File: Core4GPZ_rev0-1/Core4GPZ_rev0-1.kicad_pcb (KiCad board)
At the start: 2 copper layers, 78.7 x 105.2 mm, 50 parts, among them IC1 MAX9926UAEE_V+, M3 MountingHole_3.2mm_M3_DIN965_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, Q1 FGD3440G2-F085, Q2 FGD3440G2-F085, U2 core4, U3 MPXHZ6250AC6T1, U4 LMV321

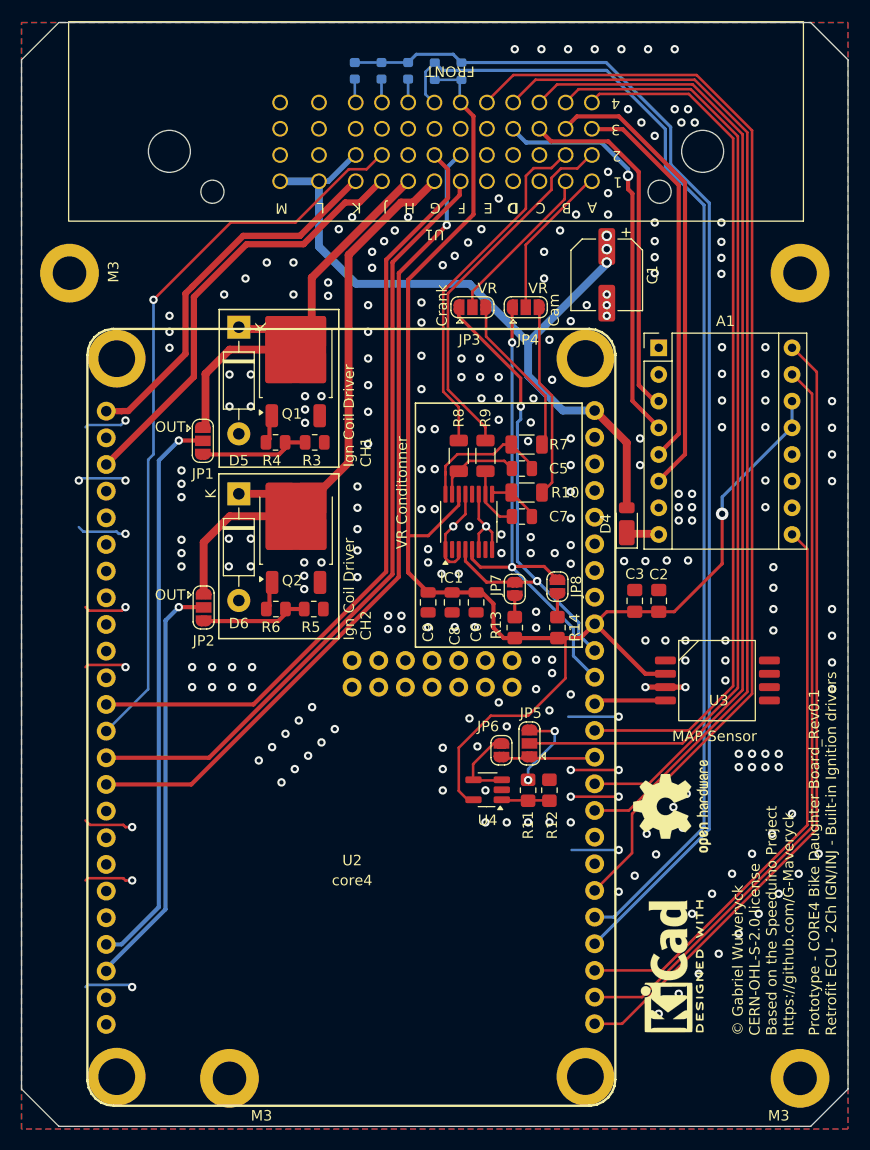
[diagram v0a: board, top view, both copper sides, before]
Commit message: Updated CAD Enclosure STL and STEP export
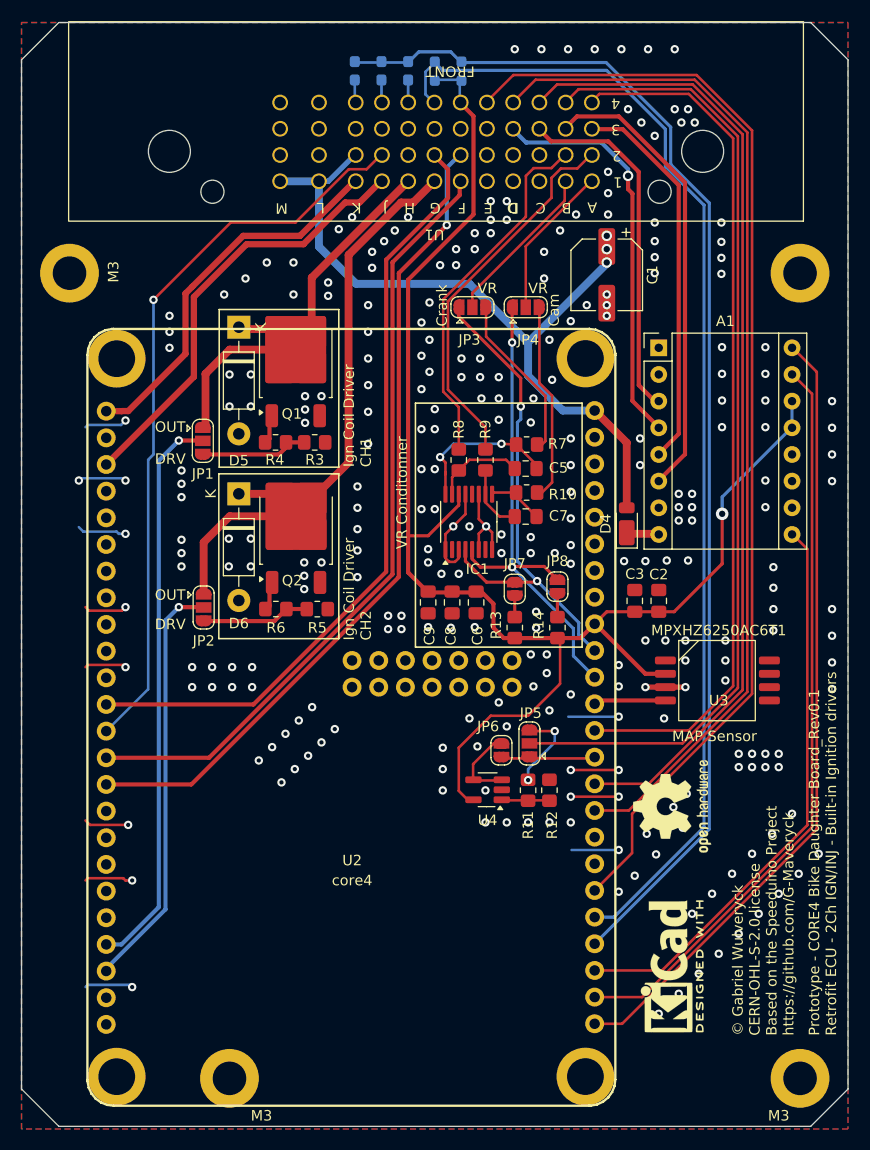
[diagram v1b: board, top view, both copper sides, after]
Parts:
- C5, C6, C7, C8, C9: footprint Capacitor_SMD:C_0805_2012Metric -> Capacitor_SMD:C_0805_2012Metric_Pad1.18x1.45mm_HandSolder
- D1, D2, D3: footprint Diode_SMD:D_0603_1608Metric -> Diode_SMD:D_0603_1608Metric_Pad1.05x0.95mm_HandSolder
- R1, R2: footprint Resistor_SMD:R_0603_1608Metric -> Resistor_SMD:R_0603_1608Metric_Pad0.98x0.95mm_HandSolder
- R10, R7, R8, R9: footprint Resistor_SMD:R_1206_3216Metric -> Resistor_SMD:R_0805_2012Metric_Pad1.20x1.40mm_HandSolder
- R3, R4, R5, R6: footprint Resistor_SMD:R_0805_2012Metric -> Resistor_SMD:R_0805_2012Metric_Pad1.20x1.40mm_HandSolder
- moved R8 0.39 mm to (119.1, 80.4)
- moved R9 0.39 mm to (121.7, 80.4)
- moved C5 0.36 mm to (125.5, 81.2)
- moved C7 0.36 mm to (125.5, 85.8)
- moved R5 0.33 mm to (105.7, 94.6)
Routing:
- net Net-(IC1-IN1+): track 13.1 -> 14.9 mm, vias 0 -> 2
- net CAM_SNSR_VR-: track 35.3 -> 36.1 mm
- net CRANK_SNSR_VR-: track 33.8 -> 34.5 mm
- net GND: track 75.2 -> 74.7 mm, vias 265 -> 275
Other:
- board text added: "DRV"

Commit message: Updated component Library with specific parts
Added "Speeduino_bike_prototype" library, with symbols and footprints.
You can add this library to your library table.
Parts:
- U1: footprint Molex_CMC_Conn:Molex_CMC_48pin_Male_Black -> Speeduino_Bike_Prototype:Molex_CMC_48pin_Male_Black
- U2: value core4 -> core4_rev1; footprint CORE4:Core4_rev1 -> Speeduino_Bike_Prototype:Core4
- U3: footprint IC_Automotive:MPXHZ6250AC6T1 -> Speeduino_Bike_Prototype:MPXHZ6250AC6T1
- moved REF** 2.46 mm to (140.9, 115.4)
- moved REF** 1.98 mm to (141.4, 128.6)
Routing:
- net GND: track 74.7 -> 72.1 mm, vias 275 -> 276
- net /INJ1_TRIG: track 36.6 -> 37.7 mm
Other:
- board text removed: "MAP Sensor"

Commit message: Updated project library, BOM and documentation
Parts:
- removed the R2 at (116.8, 43.4)
- removed the R5 at (105.7, 94.6)
- removed the R6 at (101.7, 94.6)
- removed the R9 at (121.7, 80.4)
- added C6: 1nF, Capacitor_SMD:C_0805_2012Metric_Pad1.18x1.45mm_HandSolder, F.Cu at (125.5, 88.0)
- added R1: 100k, Resistor_SMD:R_0805_2012Metric_Pad1.20x1.40mm_HandSolder, B.Cu at (116.8, 42.9)
- added R11: 10k, Resistor_SMD:R_1206_3216Metric_Pad1.30x1.75mm_HandSolder, F.Cu at (121.7, 79.9)
- added R12: 10k, Resistor_SMD:R_1206_3216Metric_Pad1.30x1.75mm_HandSolder, F.Cu at (126.0, 83.6)
- added R7: 10k, Resistor_SMD:R_0805_2012Metric_Pad1.20x1.40mm_HandSolder, F.Cu at (105.7, 94.6)
- D1, D2, D3: value D -> 1N4448WX-TP; footprint Diode_SMD:D_0603_1608Metric_Pad1.05x0.95mm_HandSolder -> Diode_SMD:D_SOD-323_HandSoldering
- R10: footprint Resistor_SMD:R_0805_2012Metric_Pad1.20x1.40mm_HandSolder -> Resistor_SMD:R_1206_3216Metric_Pad1.30x1.75mm_HandSolder
- R2: renamed from R1; footprint Resistor_SMD:R_0603_1608Metric_Pad0.98x0.95mm_HandSolder -> Resistor_SMD:R_0805_2012Metric_Pad1.20x1.40mm_HandSolder
- R8: value 10k -> 1k
- R9: renamed from R7; footprint Resistor_SMD:R_0805_2012Metric_Pad1.20x1.40mm_HandSolder -> Resistor_SMD:R_1206_3216Metric_Pad1.30x1.75mm_HandSolder
- U1: footprint Speeduino_Bike_Prototype:Molex_CMC_48pin_Male_Black -> Bike_Prototype_LIB:Molex_CMC_48pin_Male_Black
- U2: footprint Speeduino_Bike_Prototype:Core4 -> Bike_Prototype_LIB:Core4
- U3: footprint Speeduino_Bike_Prototype:MPXHZ6250AC6T1 -> Bike_Prototype_LIB:MPXHZ6250AC6T1
- moved R8 22.4 mm to (101.9, 94.6), turned to 0 degrees
- moved R10 7.43 mm to (119.1, 79.9), turned to -90 degrees
- moved D1 0.55 mm to (109.2, 42.8)
- moved D2 0.51 mm to (111.8, 42.8)
- moved D3 0.51 mm to (114.3, 42.8)
- moved R2 0.43 mm to (119.4, 42.9)
- moved R14 0.13 mm to (128.5, 96.2)
- moved U2 0.08 mm to (85.6, 75.8)
- moved U3 0.07 mm to (143.9, 100.7)
- renumbered C5 to C4, C6 to C5, C8 to C7, C9 to C8, JP5 to JP1, JP6 to JP2, JP1 to JP3, JP2 to JP4, JP3 to JP5, JP4 to JP6, R11 to R3, R12 to R4, R3 to R5, R4 to R6
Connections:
- JP4 pad 3: Net-(JP2-B) (its old number) -> Net-(JP4-B)
- JP6 pad 3: Net-(JP4-B) -> Net-(JP6-B)
- R10 pad 1: Net-(JP4-B) -> CRANK_SNSR_VR-
- R10 pad 2: Net-(IC1-IN2+) -> Net-(IC1-IN1-)
- R8 pad 1: CRANK_SNSR_VR- -> Net-(Q2-G)
- R8 pad 2: Net-(IC1-IN1-) -> Net-(JP4-B)
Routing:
- net Net-(JP6-B): track 0.00 -> 19.4 mm
- net Net-(JP2-B) (its old number): track 10.3 -> 0.00 mm
- net Net-(JP4-B): track 19.2 -> 10.3 mm
- net Net-(IC1-IN2+): track 5.18 -> 7.53 mm
- net Net-(IC1-IN2-): track 6.32 -> 8.61 mm
- net Net-(IC1-IN1+): track 14.9 -> 13.6 mm, vias 2 -> 0
- net CRANK_SNSR_VR-: track 34.5 -> 33.4 mm
- net CAM_SNSR_VR-: track 36.1 -> 35.0 mm
- net SHIFT+: track 111.6 -> 112.7 mm
- net GND: track 72.1 -> 72.2 mm, vias 276 -> 275
